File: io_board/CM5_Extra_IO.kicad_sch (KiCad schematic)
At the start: 15 parts, among them J10 BM04B-GHS-TBT_LF__SN_, J12 BM04B-GHS-TBT_LF__SN_, J13 BM04B-GHS-TBT_LF__SN_, J15 BM04B-GHS-TBT_LF__SN_, J17 BM08B-GHS-TBT_LF__SN_, J6 USB1135-15-9-L-B, J9 BM04B-GHS-TBT_LF__SN_, U2 TPS631000DRLR

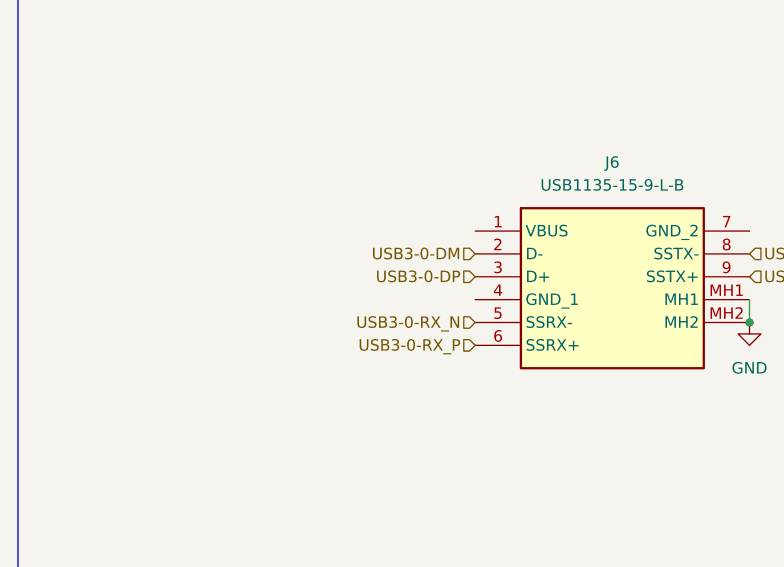
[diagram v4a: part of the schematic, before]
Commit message: Connected USB 3.0 and added part number for PCIe.
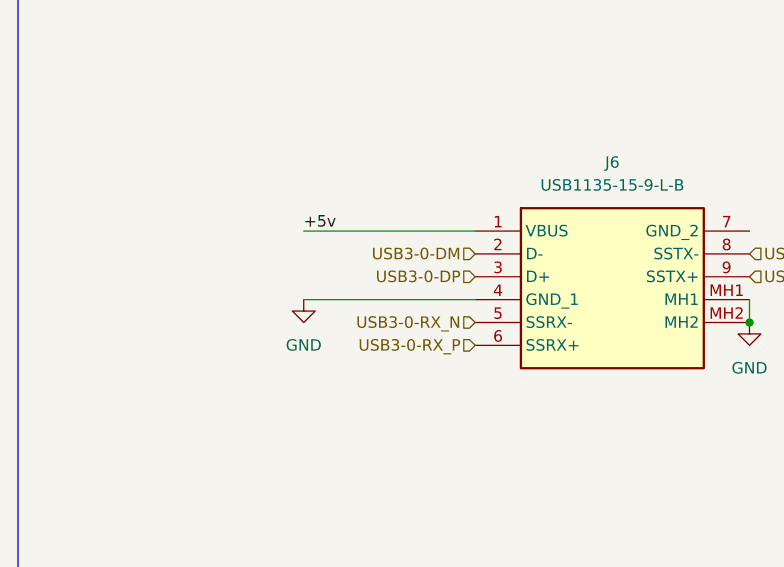
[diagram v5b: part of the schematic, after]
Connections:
- net +5v: now also J6.1 (VBUS)
- net GND: now also J6.4 (GND_1)
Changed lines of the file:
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@@
+	(wire
+		(pts
+			(xy 50.8 64.77) (xy 69.85 64.77)
+		)
+		(stroke
+			(width 0)
+			(type default)
+		)
+	)
 	(wire
 		(pts
@@
 		(pts
 			(xy 58.42 137.16) (xy 55.88 137.16)
+		)
+		(stroke
+			(width 0)
+			(type default)
+		)
+	)
+	(wire
+		(pts
+			(xy 50.8 57.15) (xy 69.85 57.15)
 		)
 		(stroke
@@
 			)
 			(justify right bottom)
+		)
+	)
+	(label "+5v"
+		(at 50.8 57.15 0)
+		(effects
+			(font
+				(size 1.27 1.27)
+			)
+			(justify left bottom)
 		)
 	)
@@
 					(unit 1)
 				)
+			)
+		)
+	)
+	(symbol
+		(lib_id "power:GND")
+		(at 50.8 64.77 0)
+		(unit 1)
+		(exclude_from_sim no)
+		(in_bom yes)
+		(on_board yes)
+		(dnp no)
+		(fields_autoplaced yes)
+		(property "Reference" "#PWR019"
+			(at 50.8 71.12 0)
+			(effects
+				(font
+					(size 1.27 1.27)
+				)
+				(hide yes)
+			)
+		)
+		(property "Value" "GND"
+			(at 50.8 69.85 0)
+			(effects
+				(font
+					(size 1.27 1.27)
+				)
+			)
+		)
+		(property "Footprint" ""
+			(at 50.8 64.77 0)
+			(effects
+				(font
+					(size 1.27 1.27)
+				)
+				(hide yes)
+			)
+		)
+		(property "Datasheet" ""
+			(at 50.8 64.77 0)
+			(effects
+				(font
+					(size 1.27 1.27)
+				)
+				(hide yes)
+			)
+		)
+		(property "Description" "Power symbol creates a global label with name \"GND\" , ground"
+			(at 50.8 64.77 0)
+			(effects
+				(font
+					(size 1.27 1.27)
+				)
+				(hide yes)
+			)
+		)
+		(pin "1"
+		)
+		(instances
+			(project "CM5IO"
+				(path "/e63e39d7-6ac0-4ffd-8aa3-1841a4541b55/1a000998-d290-4943-9ac8-07307b2fbf9f"
+					(reference "#PWR019")
+					(unit 1)
+				)
